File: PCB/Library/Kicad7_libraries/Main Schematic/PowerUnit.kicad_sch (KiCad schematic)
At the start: 22 parts, among them J2 USB_B_Micro, Q3 Q_PMOS_DGS, U4 MCP73831-2-OT, U5 TPS61200DRC, U6 LM117_TO3

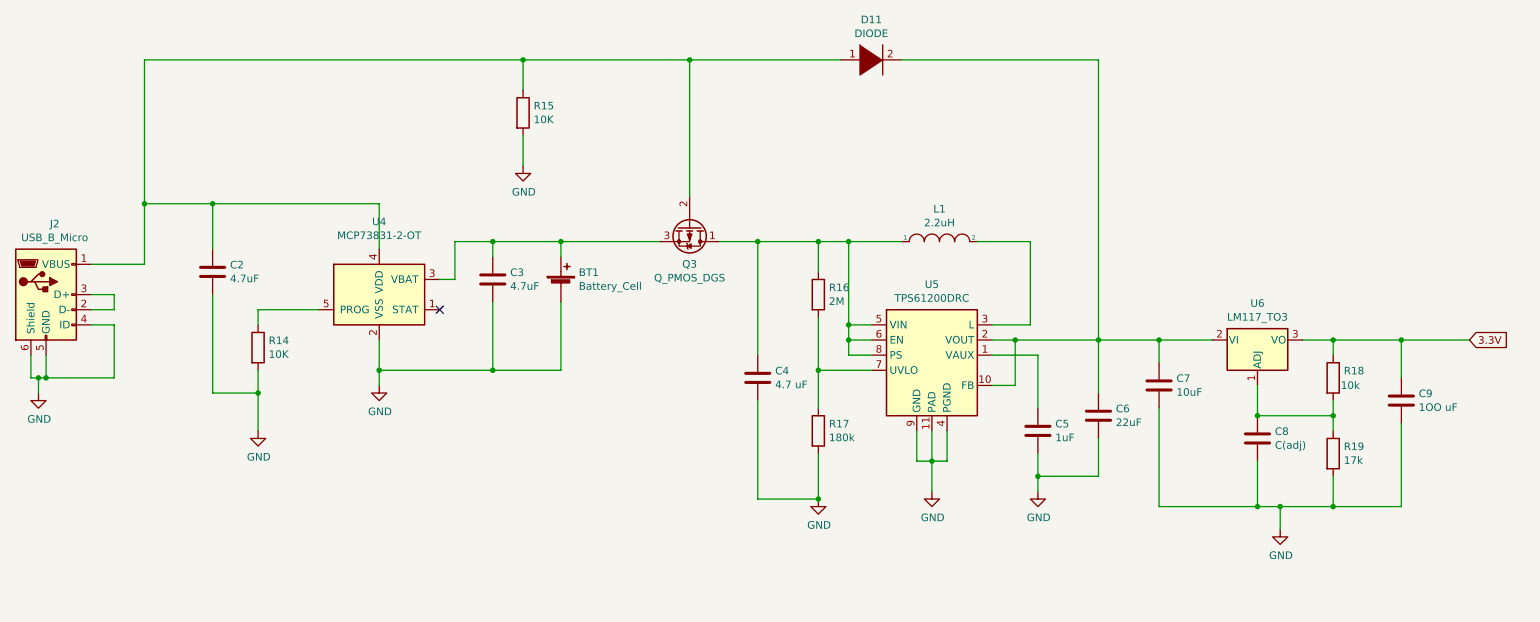
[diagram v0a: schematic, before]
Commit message: I recreated our schematics into hierachy sheets instead of individual sheets
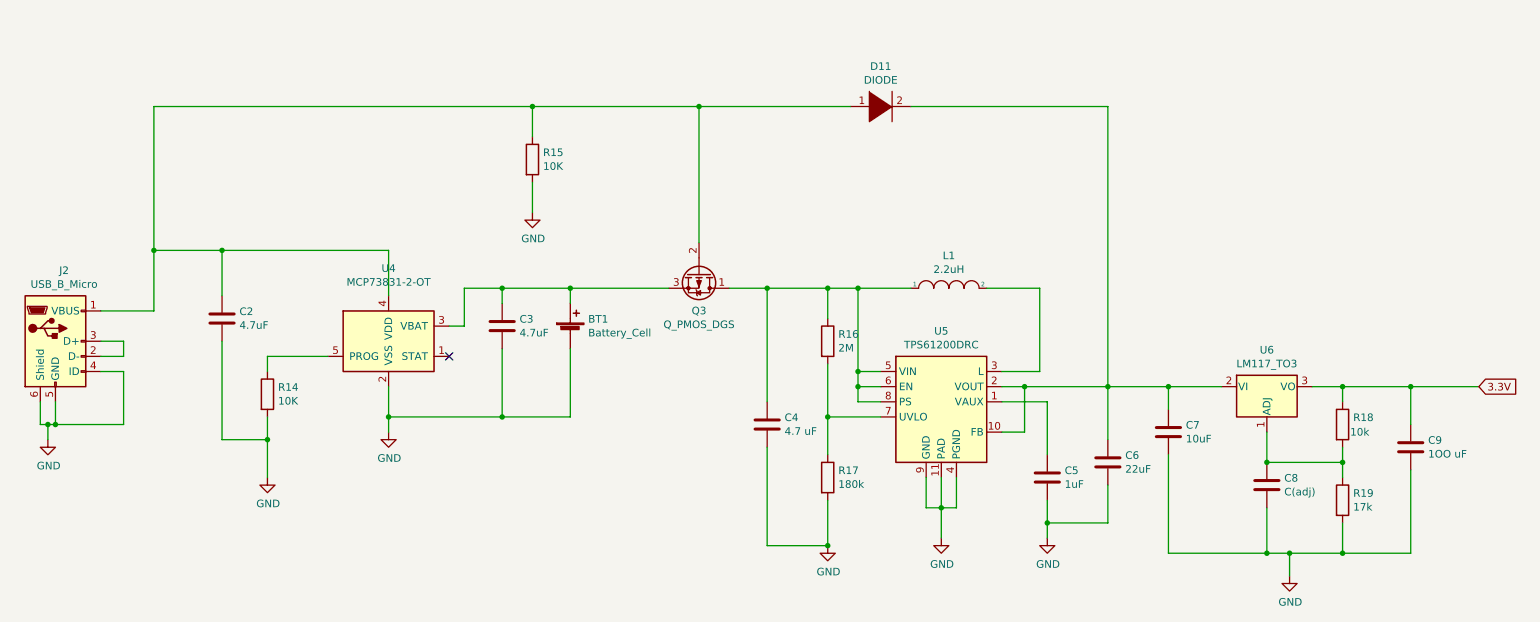
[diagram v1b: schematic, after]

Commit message: updated sche
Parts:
- removed J2: USB_B_Micro, symbol Connector:USB_B_Micro
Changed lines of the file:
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@@
   (junction (at 107.95 95.4024) (diameter 0) (color 0 0 0 0)
   )
-  (junction (at 31.75 118.2624) (diameter 0) (color 0 0 0 0)
-  )
   (junction (at 236.22 124.6124) (diameter 0) (color 0 0 0 0)
   )
@@
   )
   (junction (at 240.03 139.8524) (diameter 0) (color 0 0 0 0)
-  )
-  (junction (at 33.02 118.2624) (diameter 0) (color 0 0 0 0)
   )
   (junction (at 248.92 139.8524) (diameter 0) (color 0 0 0 0)
@@
     (stroke (width 0) (type default))
   )
-  (wire (pts (xy 30.48 118.2624) (xy 30.48 114.4524))
-    (stroke (width 0) (type default))
-  )
   (wire (pts (xy 152.4 138.5824) (xy 162.56 138.5824))
     (stroke (width 0) (type default))
   )
-  (wire (pts (xy 33.02 118.2624) (xy 33.02 114.4524))
-    (stroke (width 0) (type default))
-  )
   (wire (pts (xy 179.07 127.1524) (xy 179.07 132.2324))
     (stroke (width 0) (type default))
@@
     (stroke (width 0) (type default))
   )
-  (wire (pts (xy 31.75 118.2624) (xy 30.48 118.2624))
-    (stroke (width 0) (type default))
-  )
   (wire (pts (xy 209.55 111.9124) (xy 219.71 111.9124))
     (stroke (width 0) (type default))
@@
     (stroke (width 0) (type default))
   )
-  (wire (pts (xy 44.45 104.2924) (xy 44.45 106.8324))
-    (stroke (width 0) (type default))
-  )
   (wire (pts (xy 88.9 116.9924) (xy 107.95 116.9924))
     (stroke (width 0) (type default))
@@
     (stroke (width 0) (type default))
   )
-  (wire (pts (xy 44.45 118.2624) (xy 33.02 118.2624))
-    (stroke (width 0) (type default))
-  )
   (wire (pts (xy 260.35 139.8524) (xy 260.35 125.8824))
     (stroke (width 0) (type default))
@@
     (stroke (width 0) (type default))
   )
-  (wire (pts (xy 44.45 109.3724) (xy 44.45 118.2624))
-    (stroke (width 0) (type default))
-  )
   (wire (pts (xy 199.39 134.7724) (xy 199.39 137.3124))
     (stroke (width 0) (type default))
@@
     (stroke (width 0) (type default))
   )
-  (wire (pts (xy 31.75 118.2624) (xy 33.02 118.2624))
-    (stroke (width 0) (type default))
-  )
   (wire (pts (xy 171.45 114.4524) (xy 167.64 114.4524))
     (stroke (width 0) (type default))
@@
     (stroke (width 0) (type default))
   )
-  (wire (pts (xy 31.75 120.8024) (xy 31.75 118.2624))
-    (stroke (width 0) (type default))
-  )
   (wire (pts (xy 167.64 111.9124) (xy 167.64 109.3724))
     (stroke (width 0) (type default))
@@
     (stroke (width 0) (type default))
   )
-  (wire (pts (xy 44.45 106.8324) (xy 40.64 106.8324))
-    (stroke (width 0) (type default))
-  )
   (wire (pts (xy 107.95 95.4024) (xy 119.38 95.4024))
     (stroke (width 0) (type default))
@@
     (stroke (width 0) (type default))
   )
-  (wire (pts (xy 40.64 109.3724) (xy 44.45 109.3724))
-    (stroke (width 0) (type default))
-  )
   (wire (pts (xy 68.58 106.8324) (xy 68.58 109.3724))
     (stroke (width 0) (type default))
@@
   )
   (wire (pts (xy 248.92 114.4524) (xy 248.92 111.9124))
-    (stroke (width 0) (type default))
-  )
-  (wire (pts (xy 40.64 104.2924) (xy 44.45 104.2924))
     (stroke (width 0) (type default))
   )
@@
         (path "/ef6f5e70-2168-4df2-b1ca-c7d9a0d51980"
           (reference "#PWR0104") (unit 1)
-        )
-      )
-    )
-  )
-  (symbol (lib_id "Connector:USB_B_Micro") (at 33.02 104.2924 0) (unit 1)
-    (in_bom yes) (on_board yes) (dnp no)
-    (property "Reference" "J2" (at 34.4678 92.4306 0)
-      (effects (font (size 1.27 1.27)))
-    )
-    (property "Value" "USB_B_Micro" (at 34.4678 94.742 0)
-      (effects (font (size 1.27 1.27)))
-    )
-    (property "Footprint" "" (at 36.83 105.5624 0)
-      (effects (font (size 1.27 1.27)) hide)
-    )
-    (property "Datasheet" "~" (at 36.83 105.5624 0)
-      (effects (font (size 1.27 1.27)) hide)
-    )
-    (pin "1")
-    (pin "2")
-    (pin "3")
-    (pin "4")
-    (pin "5")
-    (pin "6")
-    (instances
-      (project "Main Schematic"
-        (path "/7e8c9ffe-1b32-4326-ae61-8877b5395b8a/98e117a5-3aeb-416f-98c5-160b7cf15fec"
-          (reference "J2") (unit 1)
-        )
-      )
-      (project "Main Schematic"
-        (path "/81c41bad-bb43-41af-b405-18d135a809b1/be77d6c5-6f74-462b-ad7c-0ffad190e576"
-          (reference "J2") (unit 1)
-        )
-      )
-      (project "PowerUnit_sch"
-        (path "/94a75581-cd2d-4b84-bb57-dd404d2f6711"
-          (reference "J2") (unit 1)
-        )
-      )
-      (project "power supplly[2803]"
-        (path "/ef6f5e70-2168-4df2-b1ca-c7d9a0d51980"
-          (reference "J2") (unit 1)
         )
       )
@@
         )
       )
-    )
-  )
-  (symbol (lib_id "power:GND") (at 31.75 120.8024 0) (unit 1)
-    (in_bom yes) (on_board yes) (dnp no)
-    (property "Reference" "#PWR015" (at 31.75 127.1524 0)
-      (effects (font (size 1.27 1.27)) hide)
-    )
-    (property "Value" "GND" (at 31.877 125.1966 0)
-      (effects (font (size 1.27 1.27)))
-    )
-    (property "Footprint" "" (at 31.75 120.8024 0)
-      (effects (font (size 1.27 1.27)) hide)
-    )
-    (property "Datasheet" "" (at 31.75 120.8024 0)
-      (effects (font (size 1.27 1.27)) hide)
-    )
-    (pin "1")
-    (instances
-      (project "Main Schematic"
-        (path "/7e8c9ffe-1b32-4326-ae61-8877b5395b8a/98e117a5-3aeb-416f-98c5-160b7cf15fec"
-          (reference "#PWR015") (unit 1)
-        )
-      )
-      (project "Main Schematic"
-        (path "/81c41bad-bb43-41af-b405-18d135a809b1/be77d6c5-6f74-462b-ad7c-0ffad190e576"
-          (reference "#PWR013") (unit 1)
-        )
-      )
-      (project "PowerUnit_sch"
-        (path "/94a75581-cd2d-4b84-bb57-dd404d2f6711"
-          (reference "#PWR015") (unit 1)
-        )
-      )
-      (project "power supplly[2803]"
-        (path "/ef6f5e70-2168-4df2-b1ca-c7d9a0d51980"
-          (reference "#PWR0105") (unit 1)
-        )
-      )
